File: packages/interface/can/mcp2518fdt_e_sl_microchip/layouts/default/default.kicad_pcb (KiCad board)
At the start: 2 copper layers, 6 parts

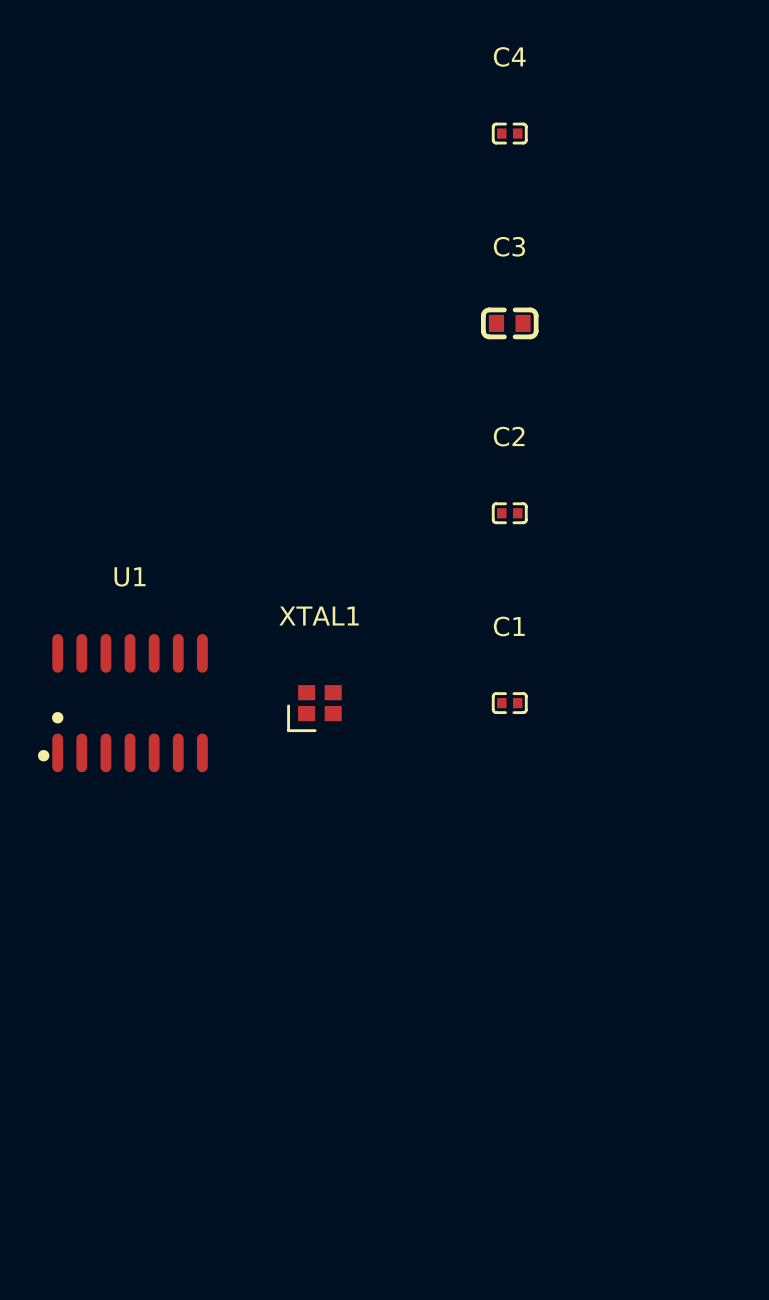
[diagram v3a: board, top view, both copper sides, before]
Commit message: MCP2518 update
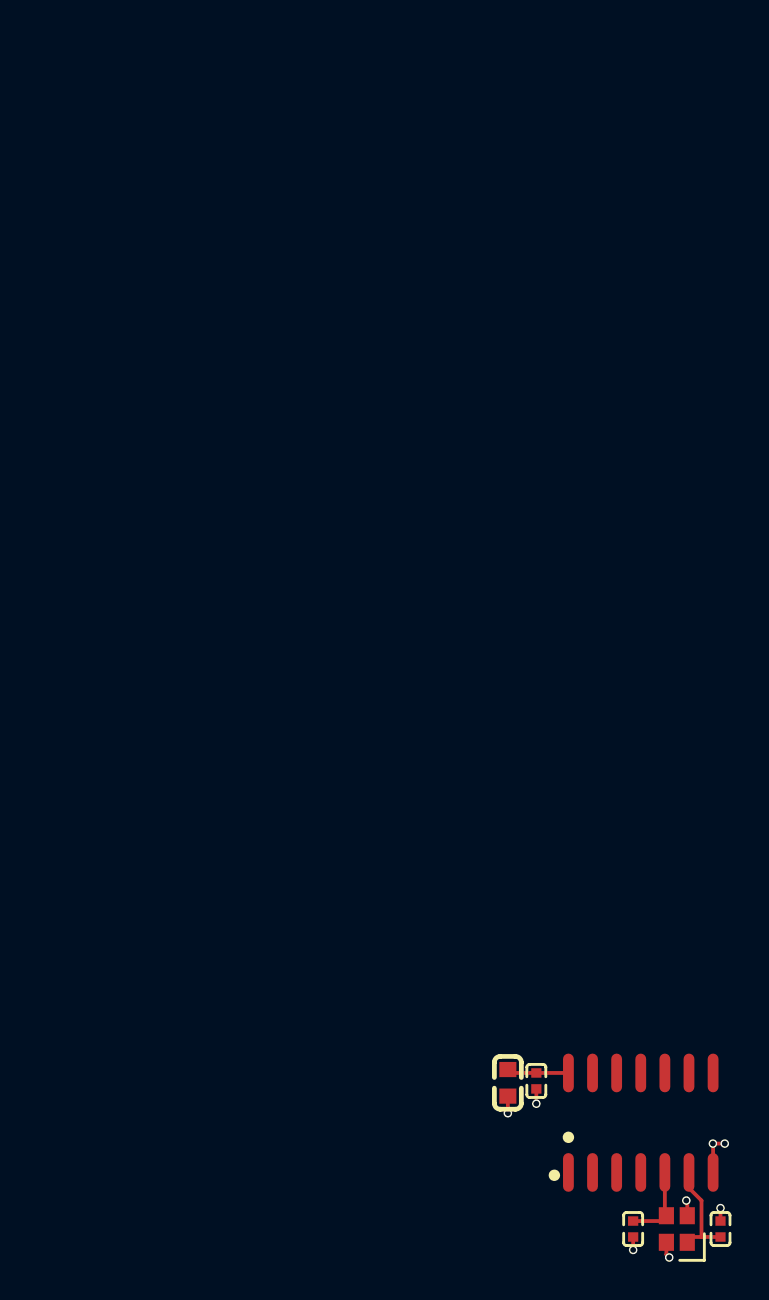
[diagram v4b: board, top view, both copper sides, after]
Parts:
- C1, C2: footprint Murata_Electronics_GRM1555C1H150JA01D:C0402 -> Murata_Electronics_GRM1555C1H220JA01D:C0402
- moved C4 49.9 mm to (21.4, 19.9), turned to -90 degrees
- moved C3 40.0 mm to (19.9, 20.0), turned to -90 degrees
- moved C2 38.3 mm to (26.5, 27.7), turned to -90 degrees
- moved U1 34.8 mm to (26.9, 22.1)
- moved XTAL1 33.5 mm to (28.8, 27.7), turned to 90 degrees
- moved C1 29.8 mm to (31.1, 27.7), turned to 90 degrees
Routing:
- net lv: track 0.00 -> 7.35 mm, vias 0 -> 8
- net 1-1: track 0.00 -> 5.54 mm
- net 1: track 0.00 -> 4.18 mm
- net hv: track 0.00 -> 3.26 mm
